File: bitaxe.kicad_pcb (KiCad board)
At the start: 4 copper layers, 59.5 x 90.2 mm, 92 parts, among them IC1 BM1387, IC2 BM1387, IC3 MIC5317, IC4 MIC5317, J1 USB_OTG, J2 Conn_01x02, J3 Conn_01x05, J4 Conn_01x02, J5 Conn_01x03, U1 DT1452-02SO-7, U2 FT231XQ, Y1 25MHz

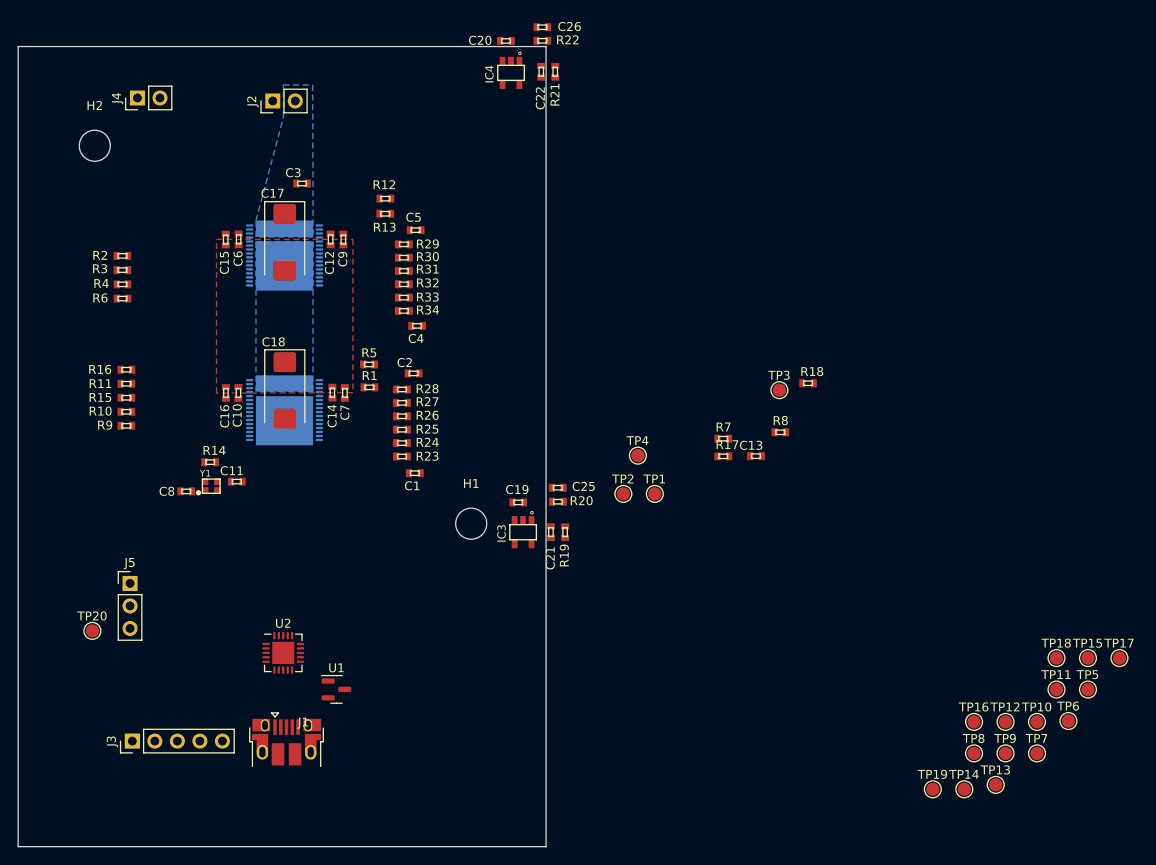
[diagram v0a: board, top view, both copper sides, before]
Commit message: routed the bitaxe!
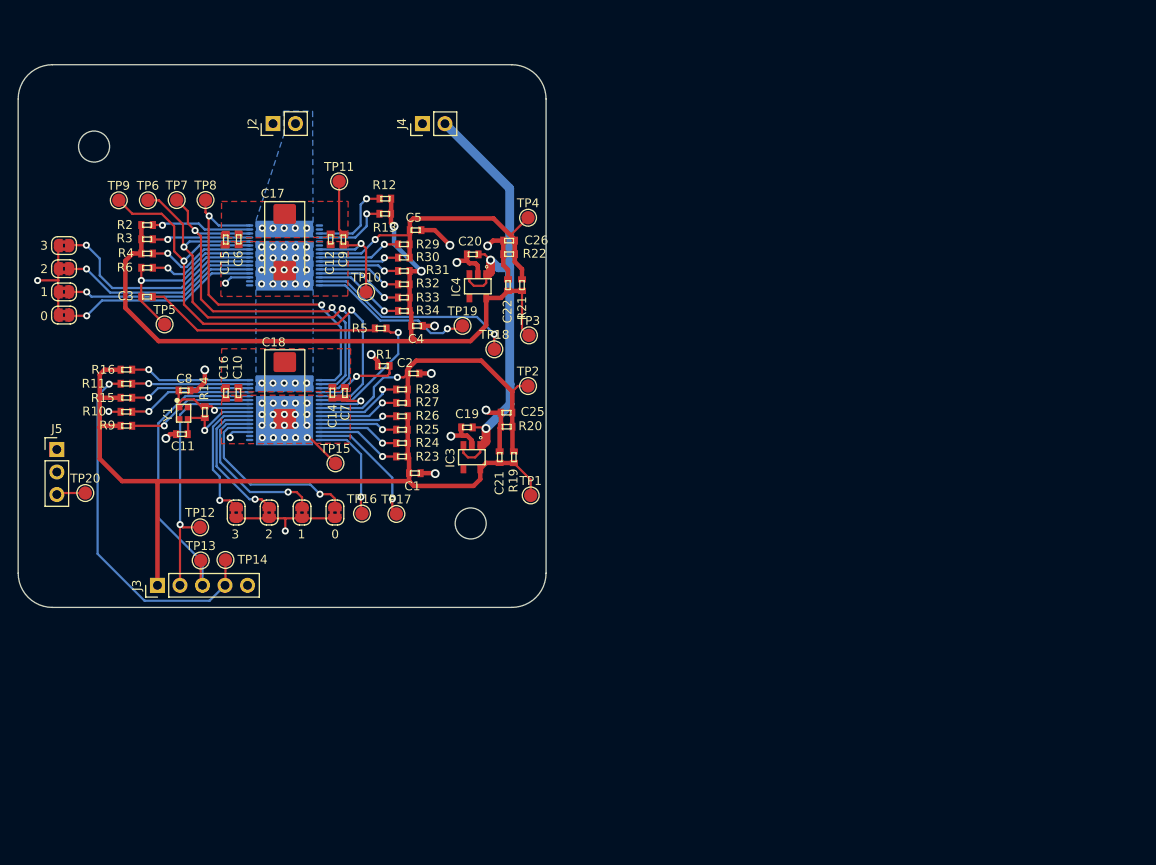
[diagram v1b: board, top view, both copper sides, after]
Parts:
- removed C13: 311-3342-1-ND, DayMiner:C0402
- removed J1: USB_OTG, DayMiner:USB_Micro-B_EDAC_UCON00686
- removed R17, R18, R8: 10k, DayMiner:R0402
- removed R7: 2.2K, DayMiner:R0402
- removed U1: DT1452-02SO-7, Package_TO_SOT_SMD:SOT-23
- removed U2: FT231XQ, Package_DFN_QFN:QFN-20-1EP_4x4mm_P0.5mm_EP2.5x2.5mm
- added JP1: SolderJumper_2_Bridged, Jumper:SolderJumper-2_P1.3mm_Bridged2Bar_RoundedPad1.0x1.5mm, F.Cu at (64.4, 66.5)
- added JP2: SolderJumper_2_Bridged, Jumper:SolderJumper-2_P1.3mm_Bridged2Bar_RoundedPad1.0x1.5mm, F.Cu at (64.4, 69.2)
- added JP3: SolderJumper_2_Bridged, Jumper:SolderJumper-2_P1.3mm_Bridged2Bar_RoundedPad1.0x1.5mm, F.Cu at (64.4, 71.8)
- added JP4: SolderJumper_2_Bridged, Jumper:SolderJumper-2_P1.3mm_Bridged2Bar_RoundedPad1.0x1.5mm, F.Cu at (64.4, 74.4)
- added JP5: SolderJumper_2_Bridged, Jumper:SolderJumper-2_P1.3mm_Bridged2Bar_RoundedPad1.0x1.5mm, F.Cu at (95.0, 96.7)
- added JP6: SolderJumper_2_Bridged, Jumper:SolderJumper-2_P1.3mm_Bridged2Bar_RoundedPad1.0x1.5mm, F.Cu at (91.3, 96.7)
- added JP7: SolderJumper_2_Bridged, Jumper:SolderJumper-2_P1.3mm_Bridged2Bar_RoundedPad1.0x1.5mm, F.Cu at (87.6, 96.7)
- added JP8: SolderJumper_2_Bridged, Jumper:SolderJumper-2_P1.3mm_Bridged2Bar_RoundedPad1.0x1.5mm, F.Cu at (83.8, 96.7)
- added kibuzzard-6222FC9E: G***, kibuzzard-6222FC9E, B.Cu at (101.7, 104.8)
- added kibuzzard-6222FCD0: G***, kibuzzard-6222FCD0, B.Cu at (92.5, 104.8)
- moved TP6 119.3 mm to (73.9, 61.4)
- moved TP9 117.9 mm to (70.6, 61.4)
- moved TP7 115.4 mm to (77.1, 61.4)
- moved TP5 112.0 mm to (75.8, 75.4)
- moved TP8 106.8 mm to (80.4, 61.4)
- moved TP11 99.2 mm to (95.5, 59.3)
- moved TP12 93.5 mm to (79.8, 98.3)
- moved TP13 93.2 mm to (79.8, 102.1)
- moved TP10 89.9 mm to (98.5, 71.8)
- moved TP15 87.7 mm to (95.0, 91.1)
- moved TP14 87.3 mm to (82.6, 102.0)
- moved TP17 83.2 mm to (101.9, 96.8)
- moved TP19 74.5 mm to (109.4, 75.6)
- moved TP16 72.9 mm to (98.0, 96.8)
- moved TP18 72.3 mm to (113.0, 78.2)
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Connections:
- IC1 pad 20: /A -> Net-(IC1-Pad20)
- IC1 pad 21: /A -> Net-(IC1-Pad21)
- IC1 pad 22: /A -> Net-(IC1-Pad22)
- IC1 pad 23: /A -> Net-(IC1-Pad23)
- IC2 pad 20: GND -> Net-(IC2-Pad20)
- IC2 pad 21: GND -> Net-(IC2-Pad21)
- IC2 pad 22: GND -> Net-(IC2-Pad22)
- IC2 pad 23: GND -> Net-(IC2-Pad23)
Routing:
- net /5V: track 0.00 -> 106.8 mm, vias 0 -> 2
- net /1V8_2: track 0.00 -> 90.2 mm
- net /1V8_1: track 0.00 -> 85.5 mm, vias 0 -> 2
- net Net-(IC1-Pad27): track 0.00 -> 59.7 mm, vias 0 -> 2
- net Net-(IC1-Pad28): track 0.00 -> 51.9 mm, vias 0 -> 2
- net GND: track 0.00 -> 49.1 mm, vias 0 -> 31
- net Net-(IC1-Pad30): track 0.00 -> 45.8 mm, vias 0 -> 2
- net /A: track 0.00 -> 42.2 mm, vias 0 -> 32
- net /RST_N: track 0.00 -> 41.8 mm, vias 0 -> 1
- net Net-(IC1-Pad32): track 0.00 -> 40.6 mm, vias 0 -> 2
- net /0V8_2: track 0.00 -> 38.5 mm, vias 0 -> 1
- net /0V8_1: track 0.00 -> 35.8 mm, vias 0 -> 1
- net /RO: track 0.00 -> 34.8 mm
- net /CI: track 0.00 -> 30.0 mm, vias 0 -> 1
- net Net-(C3-Pad2): track 0.00 -> 26.7 mm
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- added copper zone on In2.Cu, net /A
- added copper zone on F.Cu, net /VIN
- added copper zone on F.Cu, net GND
- added copper zone on In1.Cu, net GND
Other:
- board size 59.5 x 90.2 mm -> 59.5 x 61.2 mm
- board text added: "+5V"
- board text added: "0"
- board text added: "1"
- board text added: "1V8"
- board text added: "2"
- board text added: "3"
- board text added: "FAN"
- board text added: "GND"
- board text added: "RST"
- board text added: "RXI"
- board text added: "SPD"
- board text added: "TXO"
- board text added: "VIN"

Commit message: updated BOM and manufacturing files
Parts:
- moved TP13 0.33 mm to (79.8, 101.7)
- moved TP14 0.30 mm to (82.6, 101.7)
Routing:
- net /A: track 42.2 -> 51.0 mm
- net GND: track 49.1 -> 53.2 mm
